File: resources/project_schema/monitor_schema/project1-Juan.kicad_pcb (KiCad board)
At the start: 2 copper layers, 24 parts, among them J1 Conn_01x02, J2 Conn_01x03, J3 Conn_01x04, J4 Conn_01x06, J5 Conn_01x03, J6 Conn_01x03, Q1 BSS138, Q2 BSS84, SW1 SW_MEC_5E, SW2 SW_MEC_5E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

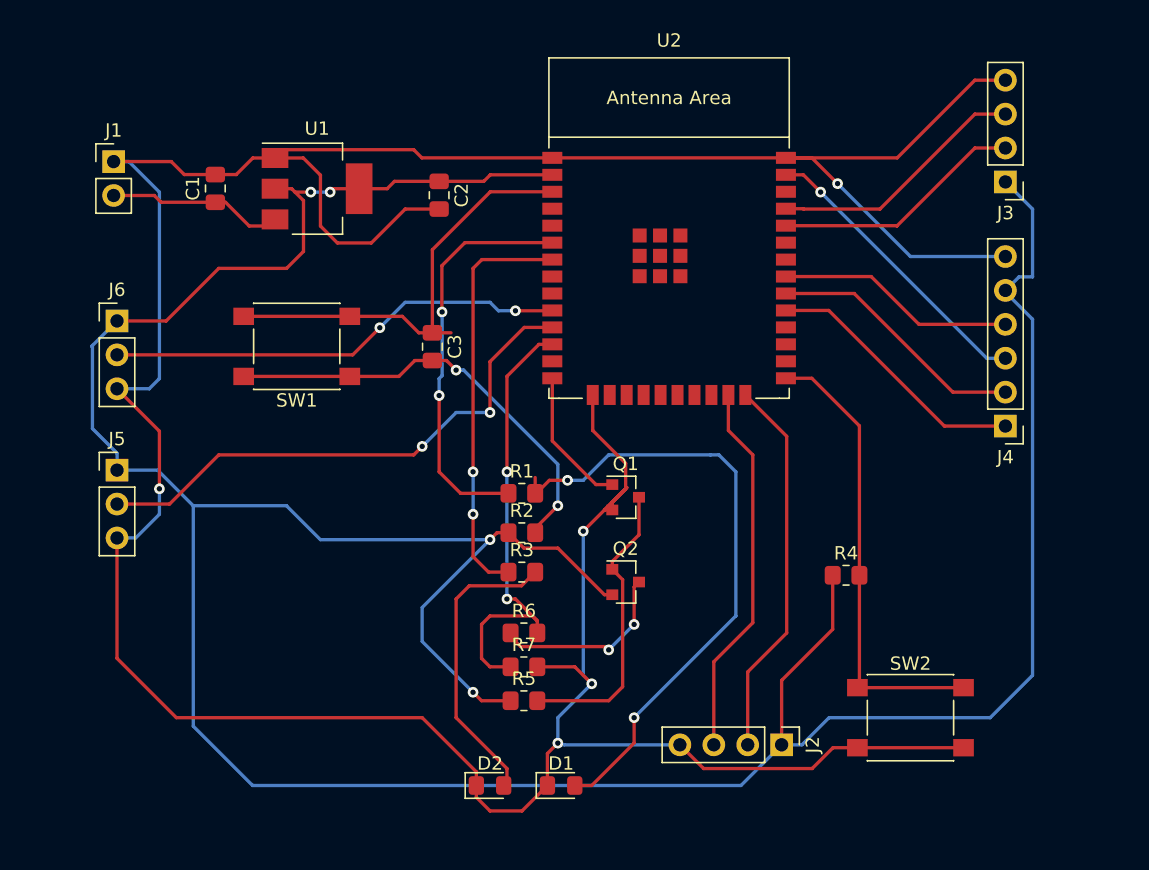
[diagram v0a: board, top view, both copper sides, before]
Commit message: PCB corregida con ancho de vias, corte y sujeción
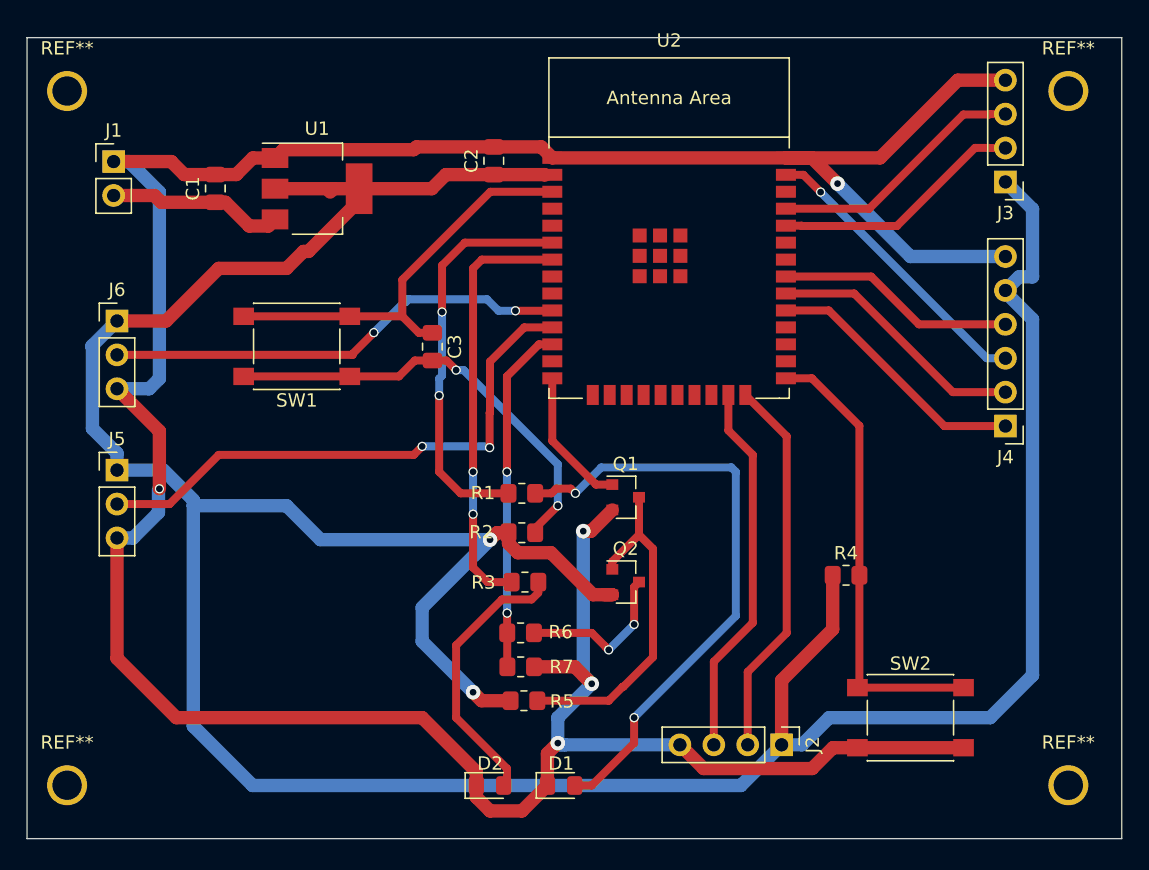
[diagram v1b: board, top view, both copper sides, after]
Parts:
- added ?: , , F.Cu at (77.5, 165.1)
- added ?: , , F.Cu at (72.0, 112.2)
- added REF**: MountingHole_2.2mm_M2, Mounting_Holes:MountingHole_2.2mm_M2, F.Cu at (150.0, 160.0)
- added REF**: MountingHole_2.2mm_M2, Mounting_Holes:MountingHole_2.2mm_M2, F.Cu at (150.0, 108.0)
- added REF**: MountingHole_2.2mm_M2, Mounting_Holes:MountingHole_2.2mm_M2, F.Cu at (75.0, 108.0)
- added REF**: MountingHole_2.2mm_M2, Mounting_Holes:MountingHole_2.2mm_M2, F.Cu at (75.0, 160.0)
- moved C2 4.84 mm to (107.0, 113.2), turned to 90 degrees
- moved R3 0.79 mm to (109.3, 144.8)
- moved R6 0.25 mm to (109.0, 148.6), turned to 180 degrees
- moved R7 0.24 mm to (109.0, 151.1)
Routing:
- net /GND: track 267.5 -> 234.4 mm
- net /esp32/BATT_V: track 34.4 -> 25.9 mm
- net Net-(Q1-Pad3): track 22.2 -> 25.9 mm
- net /Vin: track 253.6 -> 256.5 mm, vias 4 -> 2
- net Net-(Q2-Pad3): track 14.1 -> 12.2 mm
- net /esp32/EN: track 33.0 -> 31.3 mm
- net Net-(D2-Pad2): track 22.4 -> 20.8 mm
- net /esp32/GNRL_PURPOSE_2: track 40.3 -> 41.9 mm
- net Net-(D1-Pad2): track 47.2 -> 45.6 mm
- net /esp32/NO_WIFI_CONNECTION: track 30.9 -> 32.0 mm
- net /esp32/GNRL_PURPOSE_1: track 34.5 -> 35.1 mm
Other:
- board outline added: 82 x 60 mm

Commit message: Change pnp transistor footprint
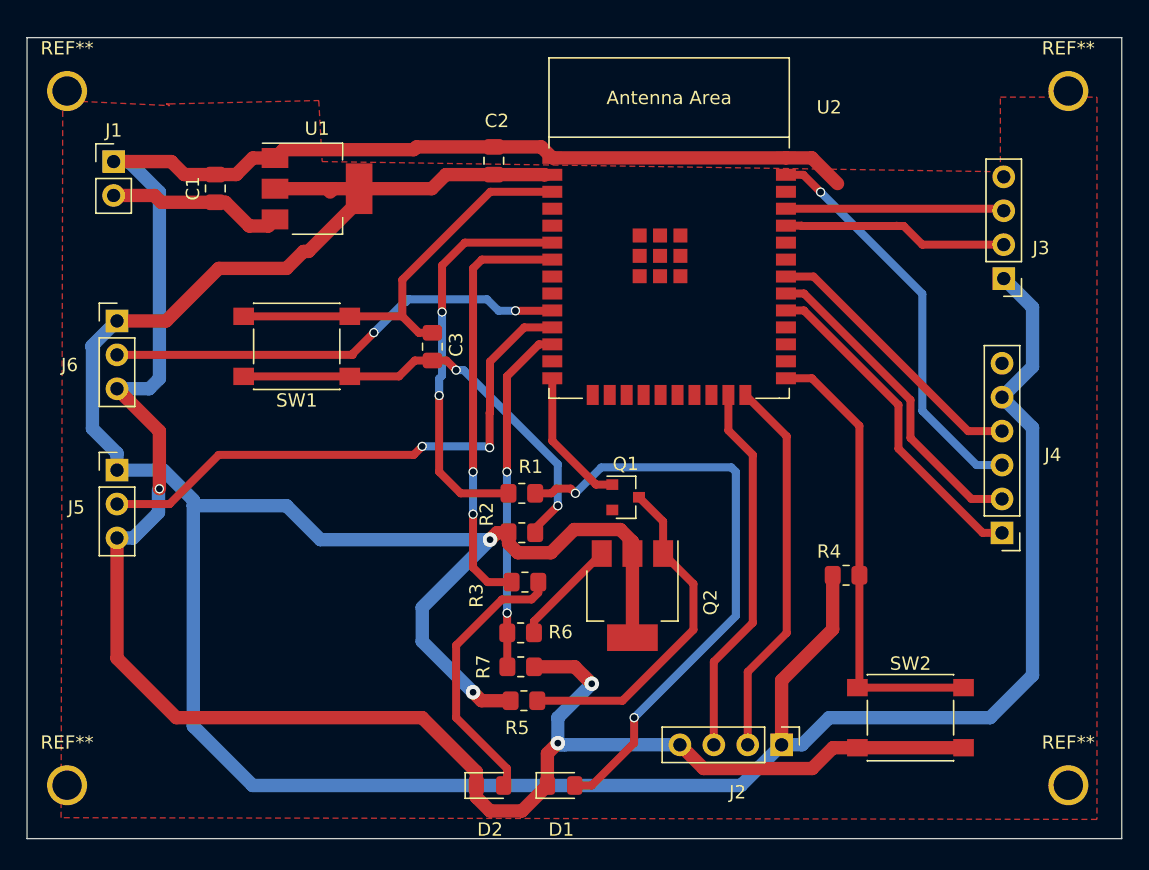
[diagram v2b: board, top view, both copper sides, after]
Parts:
- Q2: value BSS84 -> IRFL9014; footprint Package_TO_SOT_SMD:SOT-23 -> Package_TO_SOT_SMD:SOT-223
- moved J4 8.01 mm to (145.0, 141.1)
- moved J3 7.24 mm to (145.2, 122.0)
- moved Q2 1.14 mm to (117.3, 145.8), turned to 270 degrees
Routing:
- net /GND: track 234.4 -> 187.1 mm, vias 5 -> 3
- net /esp32/MOSI: track 22.1 -> 30.3 mm
- net /esp32/CS: track 20.0 -> 25.0 mm
- net /esp32/CLK: track 19.5 -> 24.2 mm
- net Net-(Q2-Pad3): track 12.2 -> 8.04 mm, vias 2 -> 0
- net /esp32/MISO: track 17.9 -> 21.0 mm
- net /esp32/RX: track 19.4 -> 16.4 mm
- net /esp32/TX: track 18.9 -> 16.9 mm
- added copper zone on F.Cu, net /GND
